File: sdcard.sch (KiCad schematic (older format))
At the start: 7 parts, among them J10 DM3D-SF

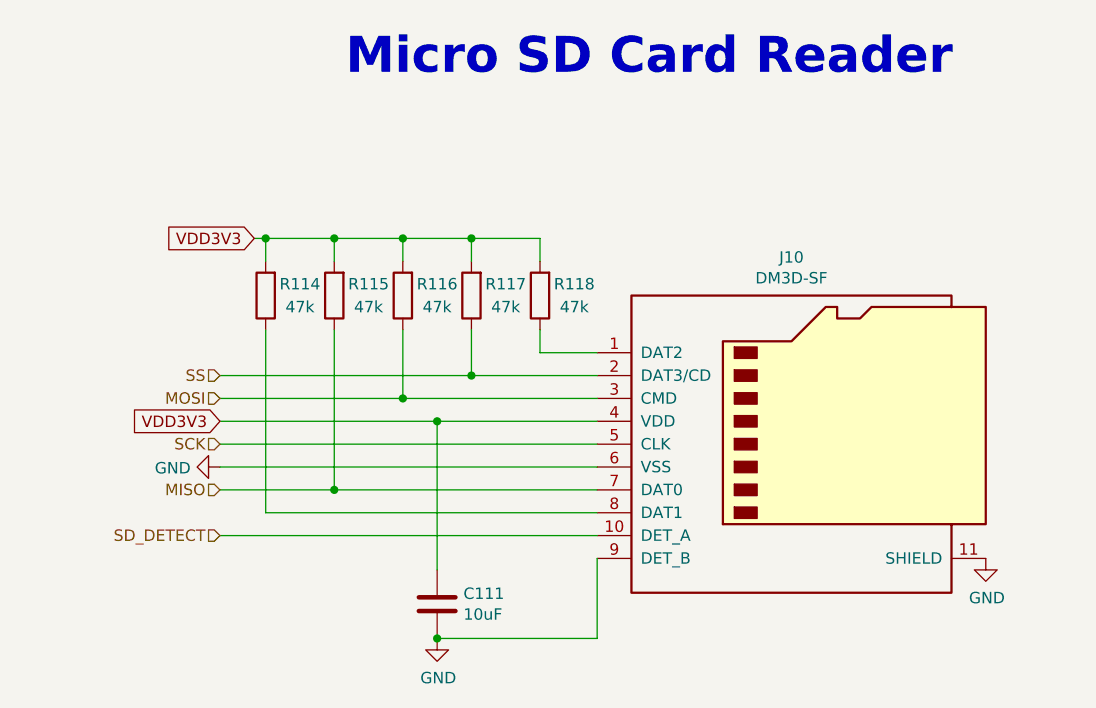
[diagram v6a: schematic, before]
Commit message: Add PU for SD_DETECT_PIN
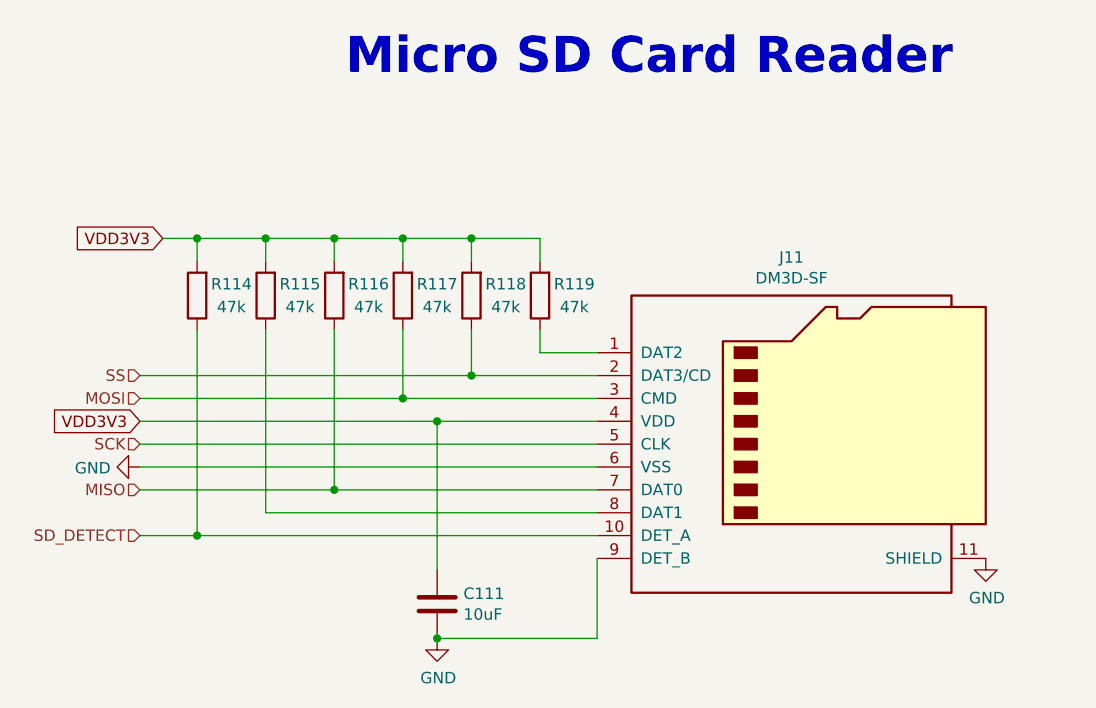
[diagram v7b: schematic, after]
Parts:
- added R114: 47k, Resistor_SMD:R_0603_1608Metric, symbol Device:R
- renumbered J10 to J11, R114 to R115, R115 to R116, R116 to R117, R117 to R118, R118 to R119
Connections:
- net SD_DETECT: now also R114.1
- net VDD3V3: now also R114.2
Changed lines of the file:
@@
 $EndDescr
 $Comp
-L Connector:Micro_SD_Card_Det_Hirose_DM3AT J10
+L Connector:Micro_SD_Card_Det_Hirose_DM3AT J11
 U 1 1 5BC78F11
 P 6000 3150
-F 0 "J10" H 5950 3967 50  0000 C CNN
+F 0 "J11" H 5950 3967 50  0000 C CNN
 F 1 "DM3D-SF" H 5950 3876 50  0000 C CNN
 F 2 "Connector_Card:microSD_HC_Hirose_DM3D-SF" H 8050 3850 50  0001 C CNN
@@
 Text Notes 4000 1550 0    157  ~ 31
 Micro SD Card Reader
-Text HLabel 3450 3350 0    50   Input ~ 0
+Text HLabel 3100 3350 0    50   Input ~ 0
 MISO
-Text HLabel 3450 2950 0    50   Input ~ 0
+Text HLabel 3100 2950 0    50   Input ~ 0
 MOSI
-Text HLabel 3450 3150 0    50   Input ~ 0
+Text HLabel 3100 3150 0    50   Input ~ 0
 SCK
-Text HLabel 3450 2850 0    50   Input ~ 0
+Text HLabel 3100 2850 0    50   Input ~ 0
 SS
 $Comp
@@
 AR Path="/5BC77F8A/5BC83407" Ref="R?"  Part="1"
 AR Path="/5BC77F8D/5BC83407" Ref="R?"  Part="1"
-AR Path="/5BC78E83/5BC83407" Ref="R118"  Part="1"
-F 0 "R118" H 4700 2450 50  0000 C CNN
+AR Path="/5BC78E83/5BC83407" Ref="R119"  Part="1"
+F 0 "R119" H 4700 2450 50  0000 C CNN
 F 1 "47k" H 4700 2550 50  0000 C CNN
 F 2 "Resistor_SMD:R_0603_1608Metric" V 4780 2500 50  0001 C CNN
@@
 	-1   0    0    1
 $EndComp
-Text HLabel 3450 3550 0    50   Input ~ 0
+Text HLabel 3100 3550 0    50   Input ~ 0
 SD_DETECT
 $Comp
 L power:GND #PWR0110
 U 1 1 5BC834C8
-P 3450 3250
-F 0 "#PWR0110" H 3450 3000 50  0001 C CNN
-F 1 "GND" V 3455 3122 50  0000 R CNN
-F 2 "" H 3450 3250 50  0001 C CNN
-F 3 "" H 3450 3250 50  0001 C CNN
-	1    3450 3250
+P 3100 3250
+F 0 "#PWR0110" H 3100 3000 50  0001 C CNN
+F 1 "GND" V 3105 3122 50  0000 R CNN
+F 2 "" H 3100 3250 50  0001 C CNN
+F 3 "" H 3100 3250 50  0001 C CNN
+	1    3100 3250
 	0    1    1    0
 $EndComp
@@
 AR Path="/5BC77F8A/5BC8393A" Ref="R?"  Part="1"
 AR Path="/5BC77F8D/5BC8393A" Ref="R?"  Part="1"
-AR Path="/5BC78E83/5BC8393A" Ref="R117"  Part="1"
-F 0 "R117" H 4400 2450 50  0000 C CNN
+AR Path="/5BC78E83/5BC8393A" Ref="R118"  Part="1"
+F 0 "R118" H 4400 2450 50  0000 C CNN
 F 1 "47k" H 4400 2550 50  0000 C CNN
 F 2 "Resistor_SMD:R_0603_1608Metric" V 4480 2500 50  0001 C CNN
@@
 AR Path="/5BC77F8A/5BC842EF" Ref="R?"  Part="1"
 AR Path="/5BC77F8D/5BC842EF" Ref="R?"  Part="1"
-AR Path="/5BC78E83/5BC842EF" Ref="R116"  Part="1"
-F 0 "R116" H 4100 2450 50  0000 C CNN
+AR Path="/5BC78E83/5BC842EF" Ref="R117"  Part="1"
+F 0 "R117" H 4100 2450 50  0000 C CNN
 F 1 "47k" H 4100 2550 50  0000 C CNN
 F 2 "Resistor_SMD:R_0603_1608Metric" V 4180 2500 50  0001 C CNN
@@
 AR Path="/5BC77F8A/5BC84424" Ref="R?"  Part="1"
 AR Path="/5BC77F8D/5BC84424" Ref="R?"  Part="1"
-AR Path="/5BC78E83/5BC84424" Ref="R115"  Part="1"
-F 0 "R115" H 3800 2450 50  0000 C CNN
+AR Path="/5BC78E83/5BC84424" Ref="R116"  Part="1"
+F 0 "R116" H 3800 2450 50  0000 C CNN
 F 1 "47k" H 3800 2550 50  0000 C CNN
 F 2 "Resistor_SMD:R_0603_1608Metric" V 3880 2500 50  0001 C CNN
@@
 Wire Wire Line
 	4850 2750 5100 2750
-Text GLabel 3600 2250 0    50   Input ~ 0
+Text GLabel 3200 2250 0    50   Input ~ 0
 VDD3V3
 Wire Wire Line
 	4850 2250 4850 2350
-Wire Wire Line
-	3450 3050 4400 3050
-Wire Wire Line
-	3450 3150 5100 3150
-Wire Wire Line
-	3450 3250 5100 3250
-Wire Wire Line
-	3450 3550 5100 3550
-Wire Wire Line
-	3450 3350 3950 3350
-Wire Wire Line
-	3450 2850 4550 2850
-Wire Wire Line
-	3450 2950 4250 2950
 $Comp
 L Device:R R?
@@
 AR Path="/5BC77F8A/5BC8859F" Ref="R?"  Part="1"
 AR Path="/5BC77F8D/5BC8859F" Ref="R?"  Part="1"
-AR Path="/5BC78E83/5BC8859F" Ref="R114"  Part="1"
-F 0 "R114" H 3500 2450 50  0000 C CNN
+AR Path="/5BC78E83/5BC8859F" Ref="R115"  Part="1"
+F 0 "R115" H 3500 2450 50  0000 C CNN
 F 1 "47k" H 3500 2550 50  0000 C CNN
 F 2 "Resistor_SMD:R_0603_1608Metric" V 3580 2500 50  0001 C CNN
@@
 	3650 2350 3650 2250
 Wire Wire Line
-	3600 2250 3650 2250
-Wire Wire Line
 	3950 2350 3950 2250
 Connection ~ 3950 2250
@@
 Wire Wire Line
 	4550 2650 4550 2850
-Connection ~ 4550 2850
 Wire Wire Line
 	4550 2850 5100 2850
 Wire Wire Line
 	4250 2650 4250 2950
-Connection ~ 4250 2950
 Wire Wire Line
 	4250 2950 5100 2950
 Wire Wire Line
 	3950 2650 3950 3350
-Connection ~ 3950 3350
 Wire Wire Line
 	3950 3350 5100 3350
@@
 Wire Wire Line
 	4400 3050 4400 3700
-Connection ~ 4400 3050
 Wire Wire Line
 	4400 3050 5100 3050
-Text GLabel 3450 3050 0    50   Input ~ 0
+Text GLabel 3100 3050 0    50   Input ~ 0
 VDD3V3
 $Comp
@@
 	5100 3650 5100 4000
 Connection ~ 4400 4000
+$Comp
+L Device:R R?
+U 1 1 5C0666FE
+P 3350 2500
+AR Path="/5BC2F52C/5C0666FE" Ref="R?"  Part="1"
+AR Path="/5BC77BE8/5C0666FE" Ref="R?"  Part="1"
+AR Path="/5BC77F87/5C0666FE" Ref="R?"  Part="1"
+AR Path="/5BC77F8A/5C0666FE" Ref="R?"  Part="1"
+AR Path="/5BC77F8D/5C0666FE" Ref="R?"  Part="1"
+AR Path="/5BC78E83/5C0666FE" Ref="R114"  Part="1"
+F 0 "R114" H 3200 2450 50  0000 C CNN
+F 1 "47k" H 3200 2550 50  0000 C CNN
+F 2 "Resistor_SMD:R_0603_1608Metric" V 3280 2500 50  0001 C CNN
+F 3 "~" H 3350 2500 50  0001 C CNN
+	1    3350 2500
+	-1   0    0    1
+$EndComp
+Connection ~ 4400 3050
+Connection ~ 3950 3350
+Connection ~ 4250 2950
+Connection ~ 4550 2850
+Wire Wire Line
+	3350 2650 3350 3550
+Wire Wire Line
+	3350 3550 5100 3550
+Wire Wire Line
+	3100 3550 3350 3550
+Connection ~ 3350 3550
+Wire Wire Line
+	3100 3350 3950 3350
+Wire Wire Line
+	3100 3250 5100 3250
+Wire Wire Line
+	3100 3150 5100 3150
+Wire Wire Line
+	3100 3050 4400 3050
+Wire Wire Line
+	3100 2950 4250 2950
+Wire Wire Line
+	3100 2850 4550 2850
+Wire Wire Line
+	3200 2250 3350 2250
+Wire Wire Line
+	3350 2350 3350 2250
+Connection ~ 3350 2250
+Wire Wire Line
+	3350 2250 3650 2250
 $EndSCHEMATC

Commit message: Improve Readability
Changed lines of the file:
@@
 L power:GND #PWR0110
 U 1 1 5BC834C8
-P 3100 3250
-F 0 "#PWR0110" H 3100 3000 50  0001 C CNN
-F 1 "GND" V 3105 3122 50  0000 R CNN
-F 2 "" H 3100 3250 50  0001 C CNN
-F 3 "" H 3100 3250 50  0001 C CNN
-	1    3100 3250
+P 3150 3250
+F 0 "#PWR0110" H 3150 3000 50  0001 C CNN
+F 1 "GND" V 3155 3122 50  0000 R CNN
+F 2 "" H 3150 3250 50  0001 C CNN
+F 3 "" H 3150 3250 50  0001 C CNN
+	1    3150 3250
 	0    1    1    0
 $EndComp
@@
 	3100 3350 3950 3350
 Wire Wire Line
-	3100 3250 5100 3250
+	3150 3250 5100 3250
 Wire Wire Line
 	3100 3150 5100 3150
